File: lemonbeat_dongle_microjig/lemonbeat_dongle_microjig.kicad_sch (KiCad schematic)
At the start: 20 parts, among them J1 Prog, J2 Main, J3 Si4467

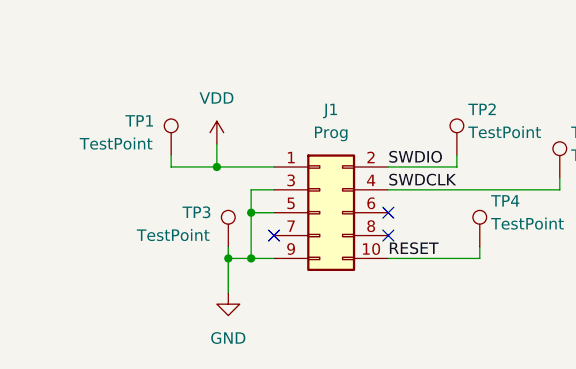
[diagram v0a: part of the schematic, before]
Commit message: dongle: microjig: routing, silk screen & LCSC part numbers
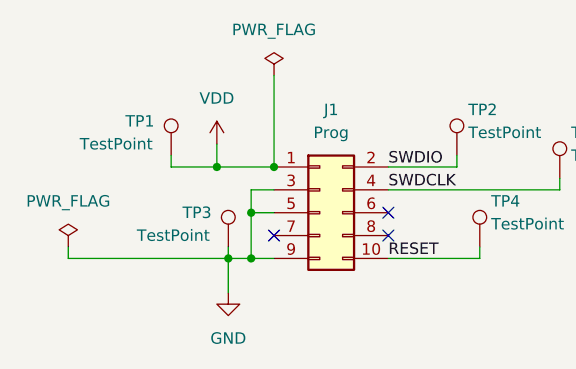
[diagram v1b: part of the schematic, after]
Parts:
- J1: LCSC (none) -> C150517; MFR Part # (none) -> 20021121-00010C4LF; Manufacturer (none) -> Amphenol ICC
- J2, J3: LCSC (none) -> C3294462; MFR Part # (none) -> PZ254-2-04-S; Manufacturer (none) -> HCTL
- TP1, TP101, TP102, TP103, TP104, TP105, TP106, TP2, TP201, TP202, TP203, TP204, TP205, TP206, TP207, TP3, TP4: LCSC (none) -> C530676

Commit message: dongle: update schematics & PCBs to KiCAD 7 & fix ERC/DRC errors & warnings
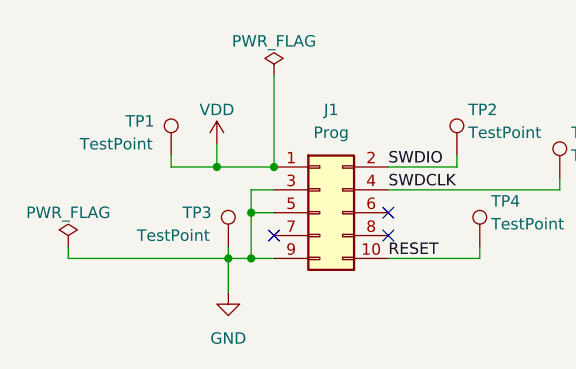
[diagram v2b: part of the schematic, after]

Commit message: dongle: microjig: use smaller pogo pins
This should mitigate the issue that pin contacts are too much off
vertically if the pins are not mounted completely upright.

Drawback is that there is there is less possible vertical compression in
the contact and M3 nuts are likely too large to mount below SMA
connector.
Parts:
- TP1, TP101, TP102, TP103, TP104, TP105, TP106, TP2, TP201, TP202, TP203, TP204, TP205, TP206, TP207, TP3, TP4: JLCPCB Alternatives (none) -> C530675: 4mm total height; C530676: 6.5mm total height; C53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; LCSC C530676 -> C530675; MFR Part # (none) -> KH-102540-DZ; Manufacturer (none) -> Shenzhen Kinghelm Elec
